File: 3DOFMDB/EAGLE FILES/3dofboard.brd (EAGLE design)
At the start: 100 x 80 mm, 139 parts, among them U1 DRV8312_DDW_44, U2 DRV8312_DDW_44, U3 DRV8312_DDW_44

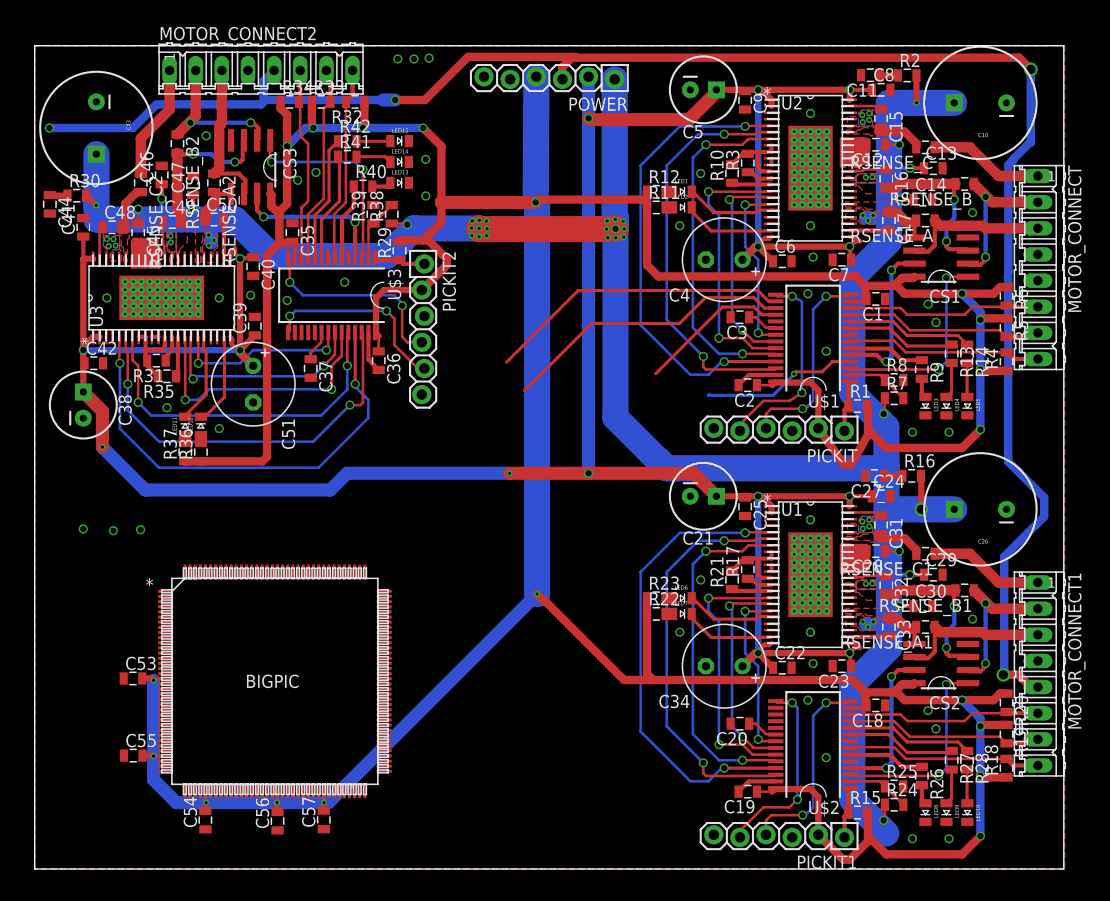
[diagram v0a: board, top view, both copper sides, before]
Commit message: Shrunk it down
Squeezed the motor driving parts together to get the thing to be an inch
and a half narrower (now about 3.5 inches wide)
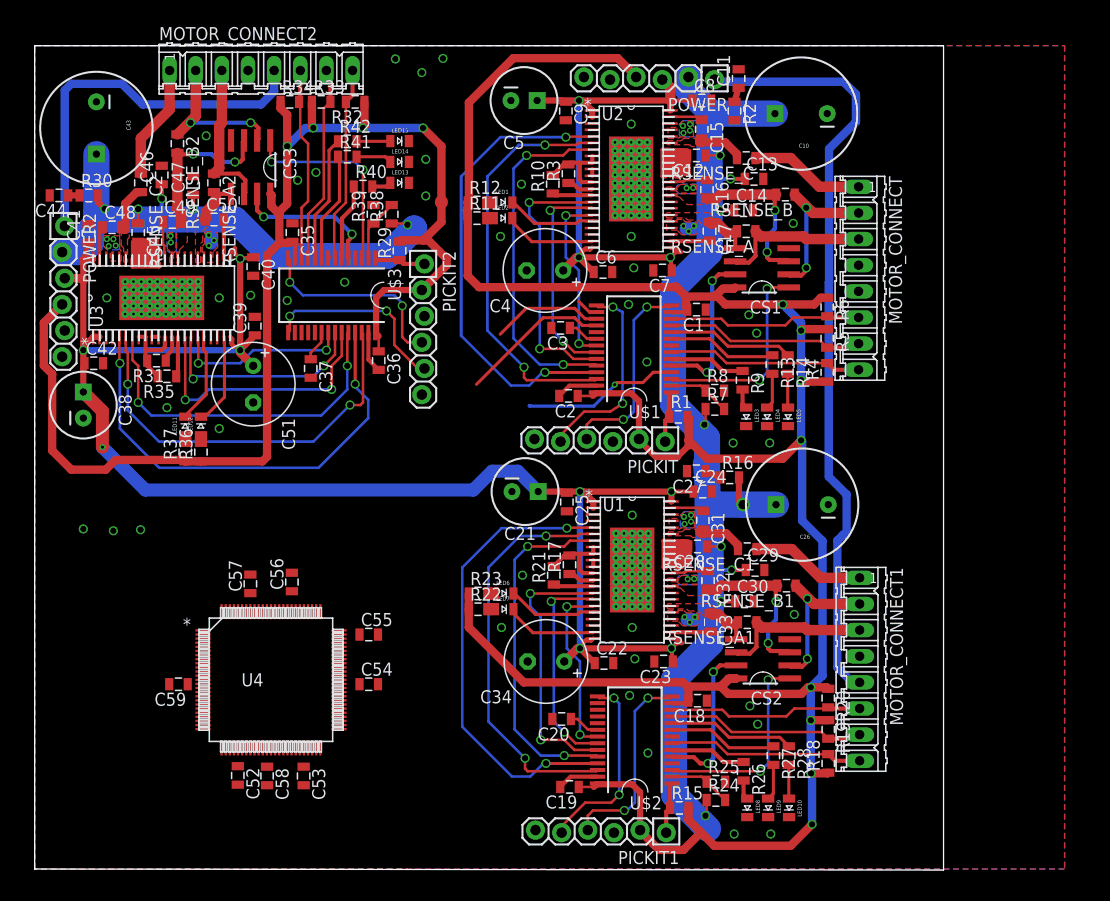
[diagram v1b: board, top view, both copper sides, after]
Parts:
- removed BIGPIC: PIC32MZXXXXEC(E/F/K)144-I/PL, PIC32:LQFP144_20X20MC
- added C52, C58, C59: 0.1u, ASL:0805
- added POWER2: (no value), ASL:1X06_LOCK
- added U4: PIC32MZXXXXEC(G/H/M)100-I/PT, PIC32_100PIN:TQFP100_12X12MC
- moved C55 25.7 mm to (32.5, 22.8)
- moved C57 24.0 mm to (21.0, 27.7)
- moved C56 23.3 mm to (25.0, 27.9)
- moved C54 20.7 mm to (32.5, 18.0), turned to 0 degrees
- moved C53 19.1 mm to (26.1, 9.04), turned to 270 degrees
- moved R16 17.7 mm to (67.5, 38.0)
- moved C1 17.5 mm to (64.3, 54.4)
- moved C12 17.5 mm to (64.3, 69.3)
- moved C14 17.5 mm to (68.9, 64.0)
- moved C16 17.5 mm to (65.3, 66.0)
- moved C2 17.5 mm to (51.9, 46.0)
- moved C3 17.5 mm to (51.1, 52.6)
- moved C5 17.5 mm to (47.5, 74.7)
- moved C6 17.5 mm to (55.2, 58.0)
- moved LED4 17.5 mm to (71.2, 43.9)
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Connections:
- removed net VDD: BIGPIC.137
- removed net VDD_2: BIGPIC.88
- removed net VDD_3: BIGPIC.107
- removed net VDD_4: BIGPIC.122
- removed net VSS: BIGPIC.136
- removed net VSS_2: BIGPIC.75
- removed net VSS_3: BIGPIC.89
- removed net VSS_4: BIGPIC.108
- new net SCK1: U$2.16, U4.58
- new net SCK2: U$3.16, U4.81
- new net SDI1: U$2.18, U4.56
- new net SDI2: U$3.18, U4.78
- new net SDO1: U$2.17, U4.57
- new net SDO2: U$3.17, U4.79
- new net SS1: U$2.4, U4.48
- new net SS2: U$3.4, U4.77
- net 12V: now also POWER.3, POWER2.3; no longer POWER.2
- net 3V3: now also C52.1, C53.1, C54.1, C55.1, C56.1, C57.1, C58.1, C59.1, POWER2.4, U4.14, U4.30, U4.37, U4.46, U4.62, U4.74, U4.83, U4.93; no longer BIGPIC.18, BIGPIC.33, BIGPIC.41, BIGPIC.55, BIGPIC.64, C53.2, C54.2, C55.2, C56.2, C57.2
- net 5V: now also POWER.1, POWER2.1; no longer POWER.3
- net GND: now also C52.2, C53.2, C54.2, C55.2, C56.2, C57.2, C58.2, C59.2, POWER2.5, POWER2.6, U4.13, U4.31, U4.36, U4.45, U4.63, U4.75, U4.84, U4.92; no longer BIGPIC.17, BIGPIC.32, BIGPIC.42, BIGPIC.54, BIGPIC.63, C53.1, C54.1, C55.1, C56.1, C57.1
- net IMESA1: now also U$2.5; no longer U$2.4
- net IMESA2: now also U$3.5; no longer U$3.4
- net SCK: now also U4.71; no longer BIGPIC.61
- net SDI: now also U4.69; no longer BIGPIC.69
- net SDO: now also U4.70; no longer BIGPIC.62
- net SS: now also U4.68; no longer BIGPIC.70
- net VBAT: now also POWER.2, POWER2.2; no longer POWER.1
- net VBUS: now also U4.51; no longer BIGPIC.73
- net VSS_5: now also U4.53; no longer BIGPIC.123
- net VUSB3V3: now also U4.52; no longer BIGPIC.74
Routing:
- net VBAT: track 266.9 -> 192.9 mm, vias 52 -> 41
- net 3V3: track 456.5 -> 383.1 mm, vias 19 -> 12
- net 12V: track 282.2 -> 214.2 mm, vias 15 -> 11
- net 5V: track 171.8 -> 112.3 mm, vias 4 -> 0
- net SCK: track 29.5 -> 2.17 mm
- net SDO: track 28.6 -> 10.8 mm
- net IMESA2: track 15.1 -> 14.3 mm
- net N$21: track 1.74 -> 1.10 mm
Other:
- board size 100 x 80 mm -> 88.3 x 80.1 mm

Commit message: Almost all components
Almost everything is down and routed, going to the bathroom
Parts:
- added C60, C61, C65, C66: 10u, ASL:0805
- added C62, C67: .01u, ASL:0805
- added C63, C68: .1u, ASL:0805
- added C64, C69: 0.47u, ASL:0805
- added J1: (no value), ASL:1X02_LOCK
- added J2: M16DUAL_ROW, ASL:2X8
- added PICKIT3: (no value), ASL:1X06_LOCK
- added R43: 10k, ASL:0805
- added SL1, SL2: (no value), ASL:1X04_LOCK
- added U$4, U$5: DRV8844PWP, drv88xx:TSSOP-28
- moved C53 4.92 mm to (31.0, 9.86)
- moved C55 4.00 mm to (34.8, 26.0), turned to 90 degrees
- moved C56 3.91 mm to (28.7, 29.1)
- moved U4 3.80 mm to (26.6, 19.6)
- moved C54 3.76 mm to (36.0, 19.2)
- moved C58 3.73 mm to (26.2, 9.78)
- moved C59 3.15 mm to (17.1, 17.8), turned to 225 degrees
- moved C57 2.85 mm to (23.7, 28.5), turned to 180 degrees
- moved C52 2.81 mm to (22.5, 8.82), turned to 220 degrees
- moved C20 0.79 mm to (50.4, 14.6)
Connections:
- removed net VSS_5: U4.53
- new net A10: J2.4, U4.29
- new net A9: J2.3, U4.28
- new net B11: J2.8, U4.35
- new net B12: J2.11, U4.41
- new net B13: J2.12, U4.42
- new net B1A_EN: U$4.26, U4.86
- new net B1A_IN: U$4.27, U4.85
- new net B1A_OUT: SL1.1, U$4.5
- new net B1B_EN: U$4.24, U4.88
- new net B1B_IN: U$4.25, U4.87
- new net B1B_OUT: SL1.2, U$4.7
- new net B2A_EN: U$4.22, U4.100
- new net B2A_IN: U$4.23, U4.99
- new net B2A_OUT: SL1.3, U$4.8
- new net B2B_EN: U$4.20, U4.4
- new net B2B_IN: U$4.21, U4.3
- new net B2B_OUT: SL1.4, U$4.10
- new net B3A_EN: U$5.26, U4.10
- new net B3A_IN: U$5.27, U4.9
- new net B3A_OUT: SL2.1, U$5.5
- new net B3B_EN: U$5.24, U4.12
- new net B3B_IN: U$5.25, U4.11
- new net B3B_OUT: SL2.2, U$5.7
- new net B4A_EN: U$5.22, U4.17
- new net B4A_IN: U$5.23, U4.16
- new net B4A_OUT: SL2.3, U$5.8
- new net B4B_EN: U$5.20, U4.19, U4.26
- new net B4B_IN: U$5.21, U4.18
- new net B4B_OUT: SL2.4, U$5.10
- new net CP1: C62.1, U$4.1
- new net CP1_1: C67.1, U$5.1
- new net CP2: C62.2, U$4.2
- new net CP2_1: C67.2, U$5.2
- new net FAULT_8844_1: U$4.18, U4.5
- new net FAULT_8844_2: U$5.18, U4.21
- new net MCLR_BP: PICKIT3.1, R43.1, U4.15
- new net N$31: C69.1, U$5.15
- new net N$38: U4.20
- new net N$60: C64.1, U$4.15
- new net PGC_BP: PICKIT3.5, U4.24
- new net PGD_BP: PICKIT3.4, U4.25
- new net RESET_8844_1: U$4.16, U4.7
- new net RESET_8844_2: U$5.16, U4.23
- new net RPB10: J2.7, U4.34
- new net RPB14: J2.13, U4.43
- new net RPB15: J2.14, U4.44
- new net RPB7: J2.2, U4.27
- new net RPB8: J2.5, U4.32
- new net RPB9: J2.6, U4.33
- new net RPD14: J2.16, U4.47
- new net RPF12: J2.10, U4.40
- new net RPF13: J2.9, U4.39
- new net SLEEP_8844_1: U$4.17, U4.6
- new net SLEEP_8844_2: U$5.17, U4.22
- new net VCP: C63.2, U$4.3
- new net VCP1: C68.2, U$5.3
- net 3V3: now also PICKIT3.2, R43.2
- net GND: now also C60.2, C61.2, C64.2, C65.2, C66.2, C69.2, J1.2, J2.1, J2.15, PICKIT3.3, U$4.14, U$4.19, U$4.28, U$4.6, U$4.9, U$4.EXP, U$5.14, U$5.19, U$5.28, U$5.6, U$5.9, U$5.EXP, U4.53
- net VBAT: now also C60.1, C61.1, C63.1, C65.1, C66.1, C68.1, J1.1, U$4.11, U$4.4, U$5.11, U$5.4
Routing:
- net 3V3: track 383.1 -> 468.0 mm, vias 12 -> 14
- net SCK: track 2.17 -> 48.4 mm
- net SS1: track 0.00 -> 36.7 mm, vias 0 -> 2
- net SS2: track 0.00 -> 35.9 mm, vias 0 -> 2
- net SDO: track 10.8 -> 46.5 mm
- net VBAT: track 192.9 -> 226.7 mm, vias 41 -> 61
- net SS: track 15.3 -> 47.8 mm, vias 1 -> 2
- net SDI: track 14.7 -> 45.5 mm
- net SCK2: track 0.00 -> 28.7 mm
- net SDI2: track 0.00 -> 28.6 mm
- net SDO2: track 0.00 -> 28.5 mm
- net SDI1: track 0.00 -> 22.3 mm
- net SDO1: track 0.00 -> 22.2 mm
- net SCK1: track 0.00 -> 22.1 mm
- net PGC_BP: track 0.00 -> 21.9 mm
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- added copper zone on layer 1, net 3V3
- added copper zone on layer 1, net B1A_OUT
- added copper zone on layer 1, net B1B_OUT
- added copper zone on layer 1, net B2A_OUT
- added copper zone on layer 1, net B2B_OUT
- added copper zone on layer 1, net B3A_OUT
- added copper zone on layer 1, net B3B_OUT
- added copper zone on layer 1, net B4A_OUT
- added copper zone on layer 1, net B4B_OUT

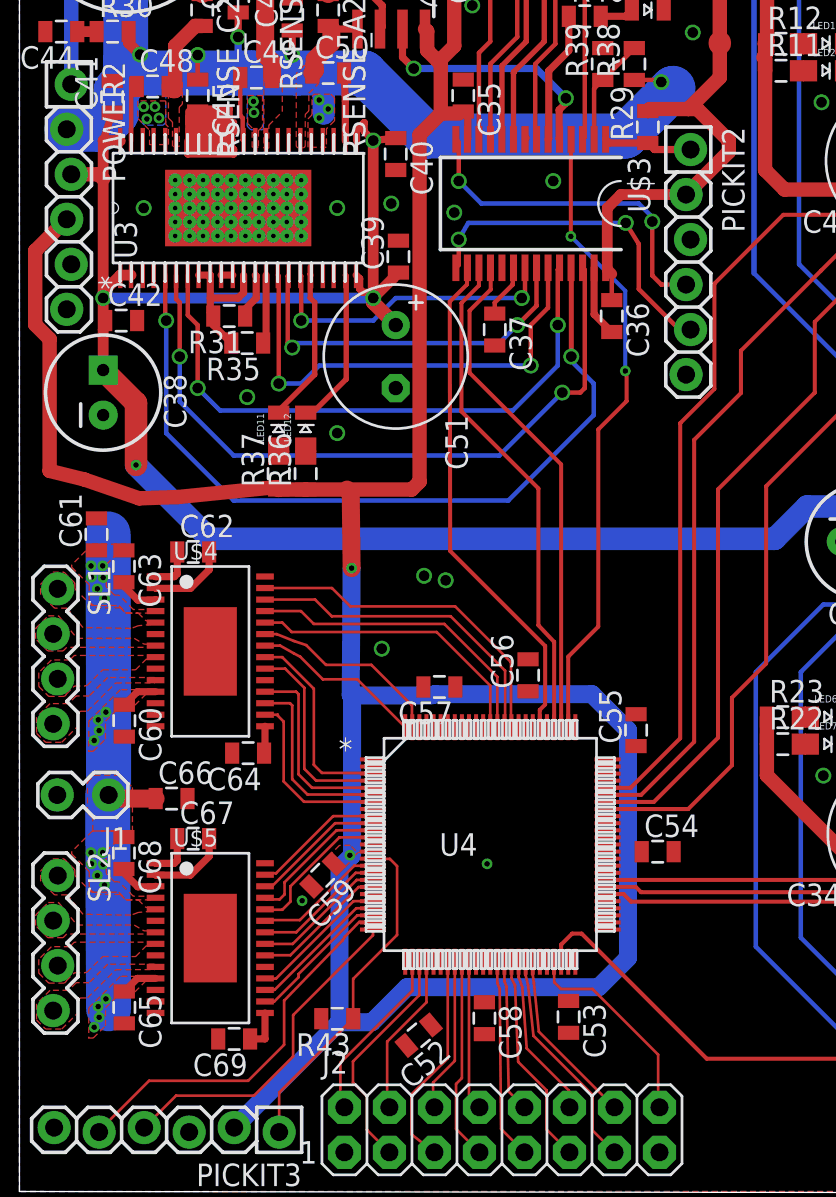
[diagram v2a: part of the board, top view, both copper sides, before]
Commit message: All components placed and routed
All components placed and routed, many DRC errors, but mostly to do with
the vias on the bottom of the DRV. Need to fix those, and make sure to
put in a bunch of ground plane vias
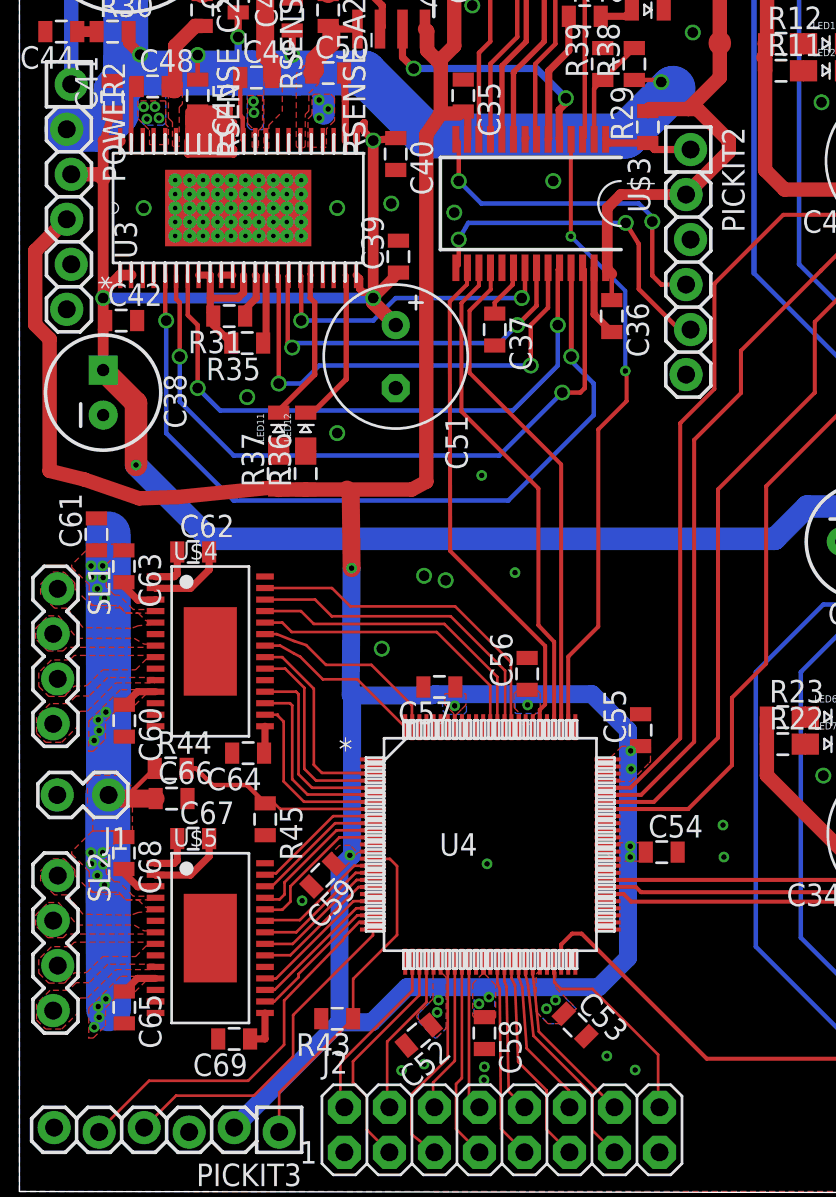
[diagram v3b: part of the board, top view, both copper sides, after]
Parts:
- added R44: 75k, ASL:0805
- added R45: 25k, ASL:0805
- moved C58 0.84 mm to (26.2, 8.94)
- moved C53 0.59 mm to (31.4, 9.39), turned to 315 degrees
- moved C55 0.25 mm to (35.1, 26.0)
- moved C54 0.23 mm to (36.2, 19.2)
- moved C56 0.09 mm to (28.7, 29.2)
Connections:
- new net BAT_MEAS_BP: R44.2, R45.1, U4.8
- net GND: now also R45.2
- net VBAT: now also R44.1
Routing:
- net BAT_MEAS_BP: track 0.00 -> 11.5 mm
- net VBAT: track 226.7 -> 229.9 mm
- net 3V3: vias 14 -> 26
- net GND: vias 44 -> 54
- added copper zone on layer 16, net 3V3

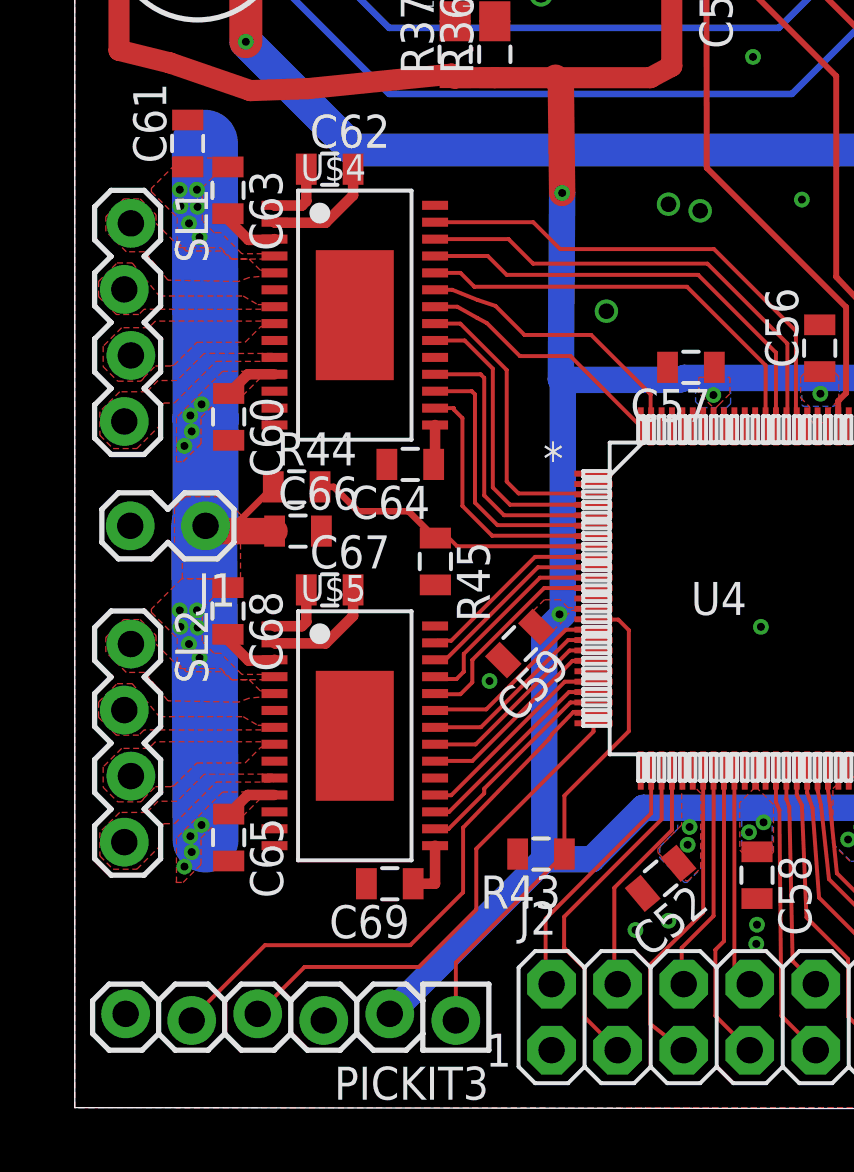
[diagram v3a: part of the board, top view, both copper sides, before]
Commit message: Improved
Minor schematic adjustments (and according routing), and 8844 polygons
fixed
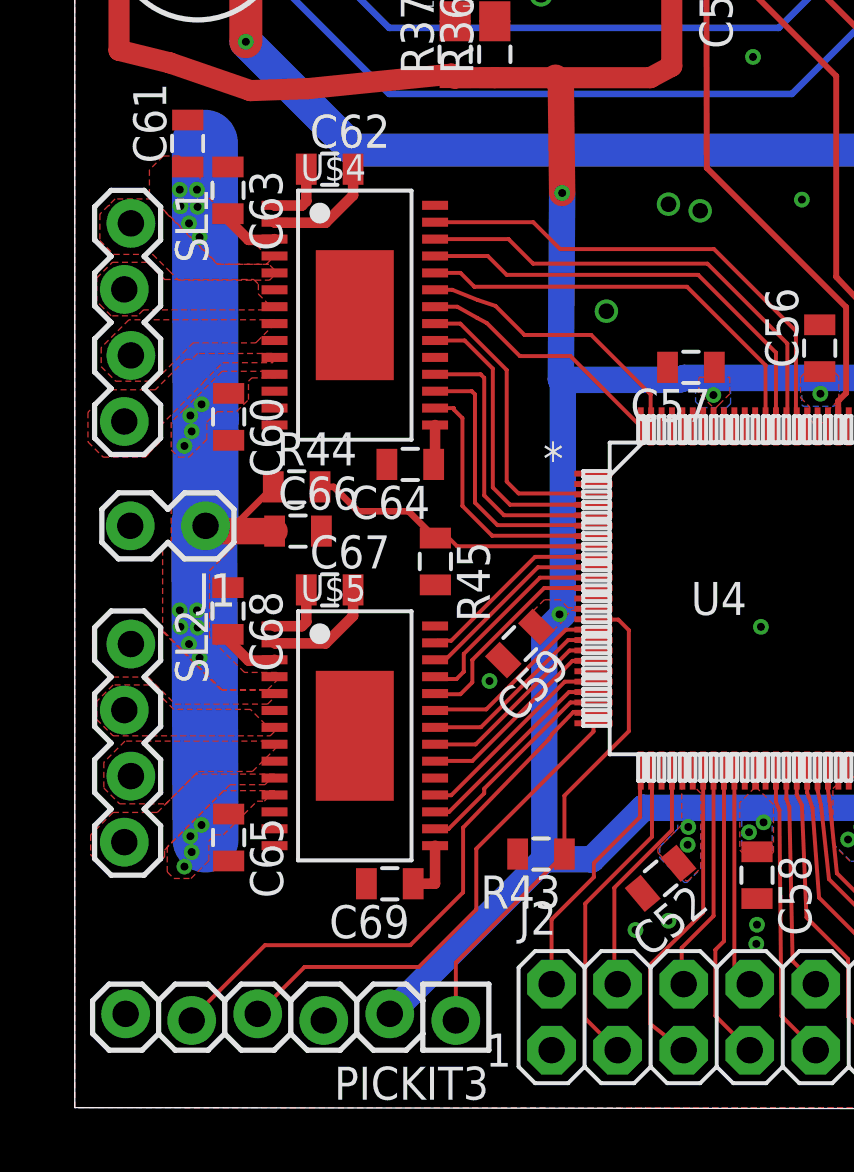
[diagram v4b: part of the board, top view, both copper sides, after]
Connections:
- new net RPB6: J2.2, U4.26
- net A9: no longer J2.3
- net B4B_EN: no longer U4.26
- net RPB7: now also J2.3; no longer J2.2
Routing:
- net A9: track 13.2 -> 0.00 mm
- net RPB6: track 0.00 -> 9.64 mm
- net VBAT: track 229.9 -> 225.8 mm
- net RPB7: track 9.99 -> 12.4 mm

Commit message: Passes DRC
Now passes DRC
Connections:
- net GND: now also U1.P$1, U1.P$10, U1.P$11, U1.P$12, U1.P$13, U1.P$14, U1.P$15, U1.P$16, U1.P$17, U1.P$18, U1.P$19, U1.P$2, U1.P$20, U1.P$21, U1.P$22, U1.P$23, U1.P$24, U1.P$25, U1.P$26, U1.P$27, U1.P$28, U1.P$29, U1.P$3, U1.P$30, U1.P$31, U1.P$32, U1.P$4, U1.P$5, U1.P$6, U1.P$7, U1.P$8, U1.P$9, U2.P$1, U2.P$10, U2.P$11, U2.P$12, U2.P$13, U2.P$14, U2.P$15, U2.P$16, U2.P$17, U2.P$18, U2.P$19, U2.P$2, U2.P$20, U2.P$21, U2.P$22, U2.P$23, U2.P$24, U2.P$25, U2.P$26, U2.P$27, U2.P$28, U2.P$29, U2.P$3, U2.P$30, U2.P$31, U2.P$32, U2.P$4, U2.P$5, U2.P$6, U2.P$7, U2.P$8, U2.P$9, U3.P$1, U3.P$10, U3.P$11, U3.P$12, U3.P$13, U3.P$14, U3.P$15, U3.P$16, U3.P$17, U3.P$18, U3.P$19, U3.P$2, U3.P$20, U3.P$21, U3.P$22, U3.P$23, U3.P$24, U3.P$25, U3.P$26, U3.P$27, U3.P$28, U3.P$29, U3.P$3, U3.P$30, U3.P$31, U3.P$32, U3.P$4, U3.P$5, U3.P$6, U3.P$7, U3.P$8, U3.P$9
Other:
- board size 88.3 x 80.1 mm -> 83.2 x 80.1 mm
